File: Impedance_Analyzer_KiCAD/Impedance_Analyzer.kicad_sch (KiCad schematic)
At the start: 39 parts, among them J1 Conn_Coaxial, J10 Conn_Coaxial, J11 Screw_Terminal_01x03, J2 Conn_Coaxial, J3 Conn_Coaxial, J4 Conn_Coaxial, J5 Conn_Coaxial, J6 Conn_Coaxial, J7 Conn_Coaxial, U1 LM358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

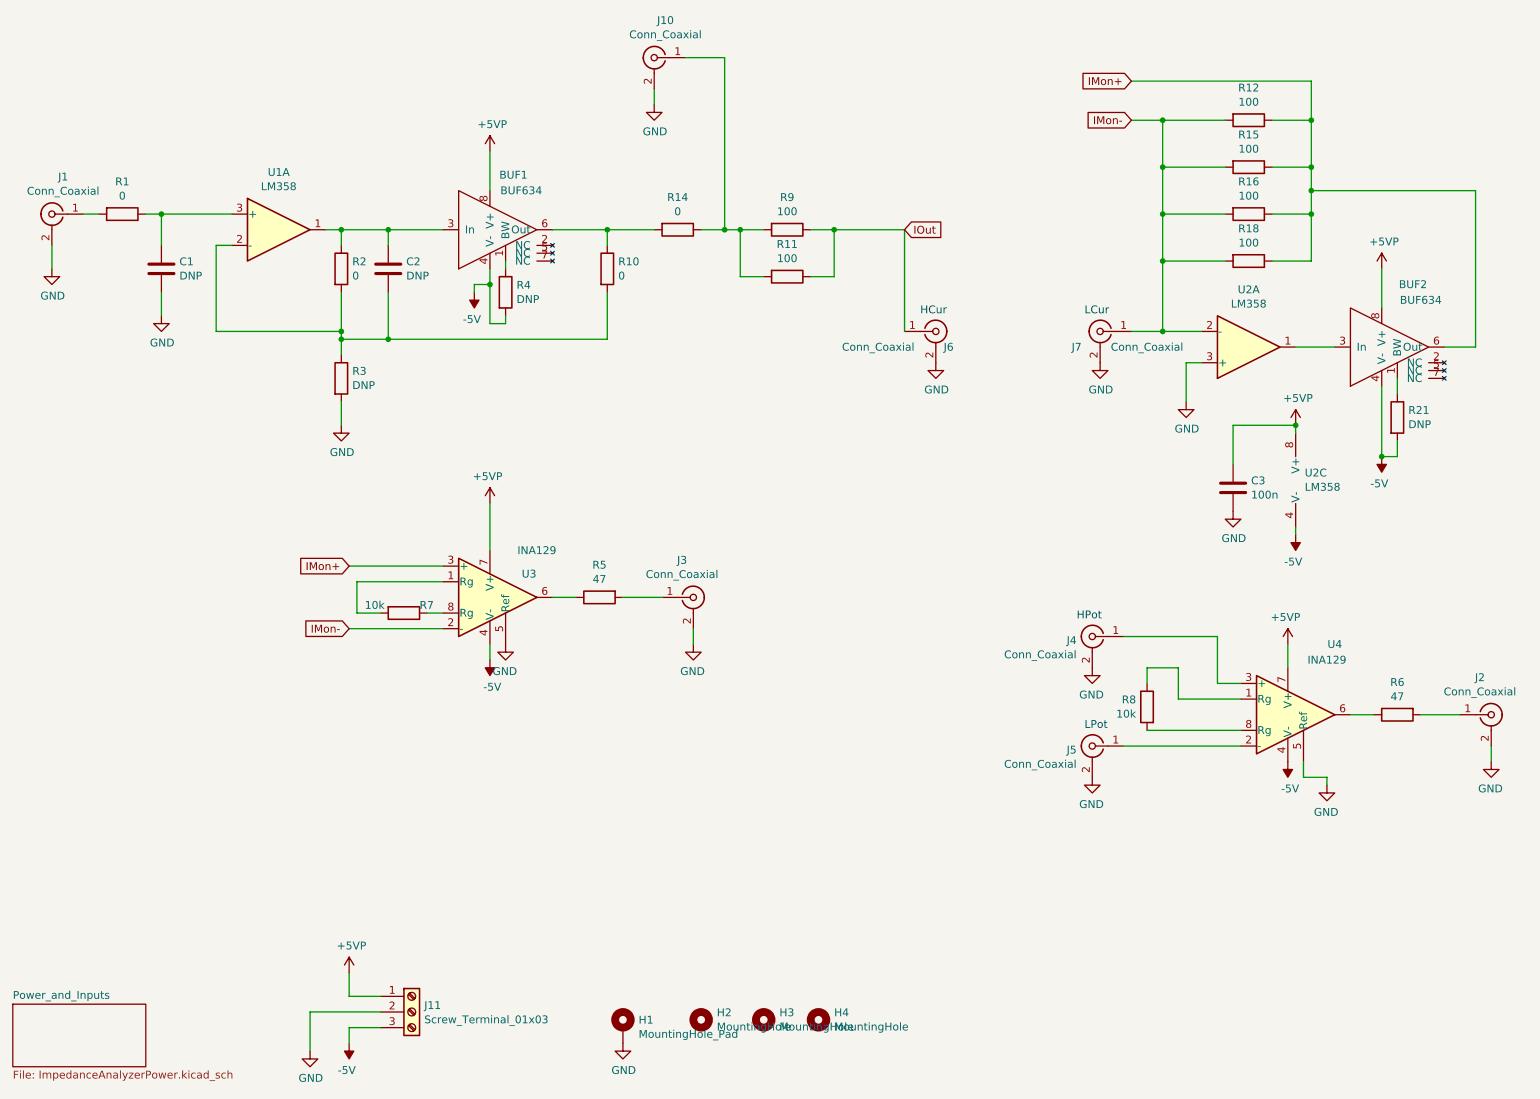
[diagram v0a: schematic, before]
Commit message: Update LTSPICE, Minor board changes
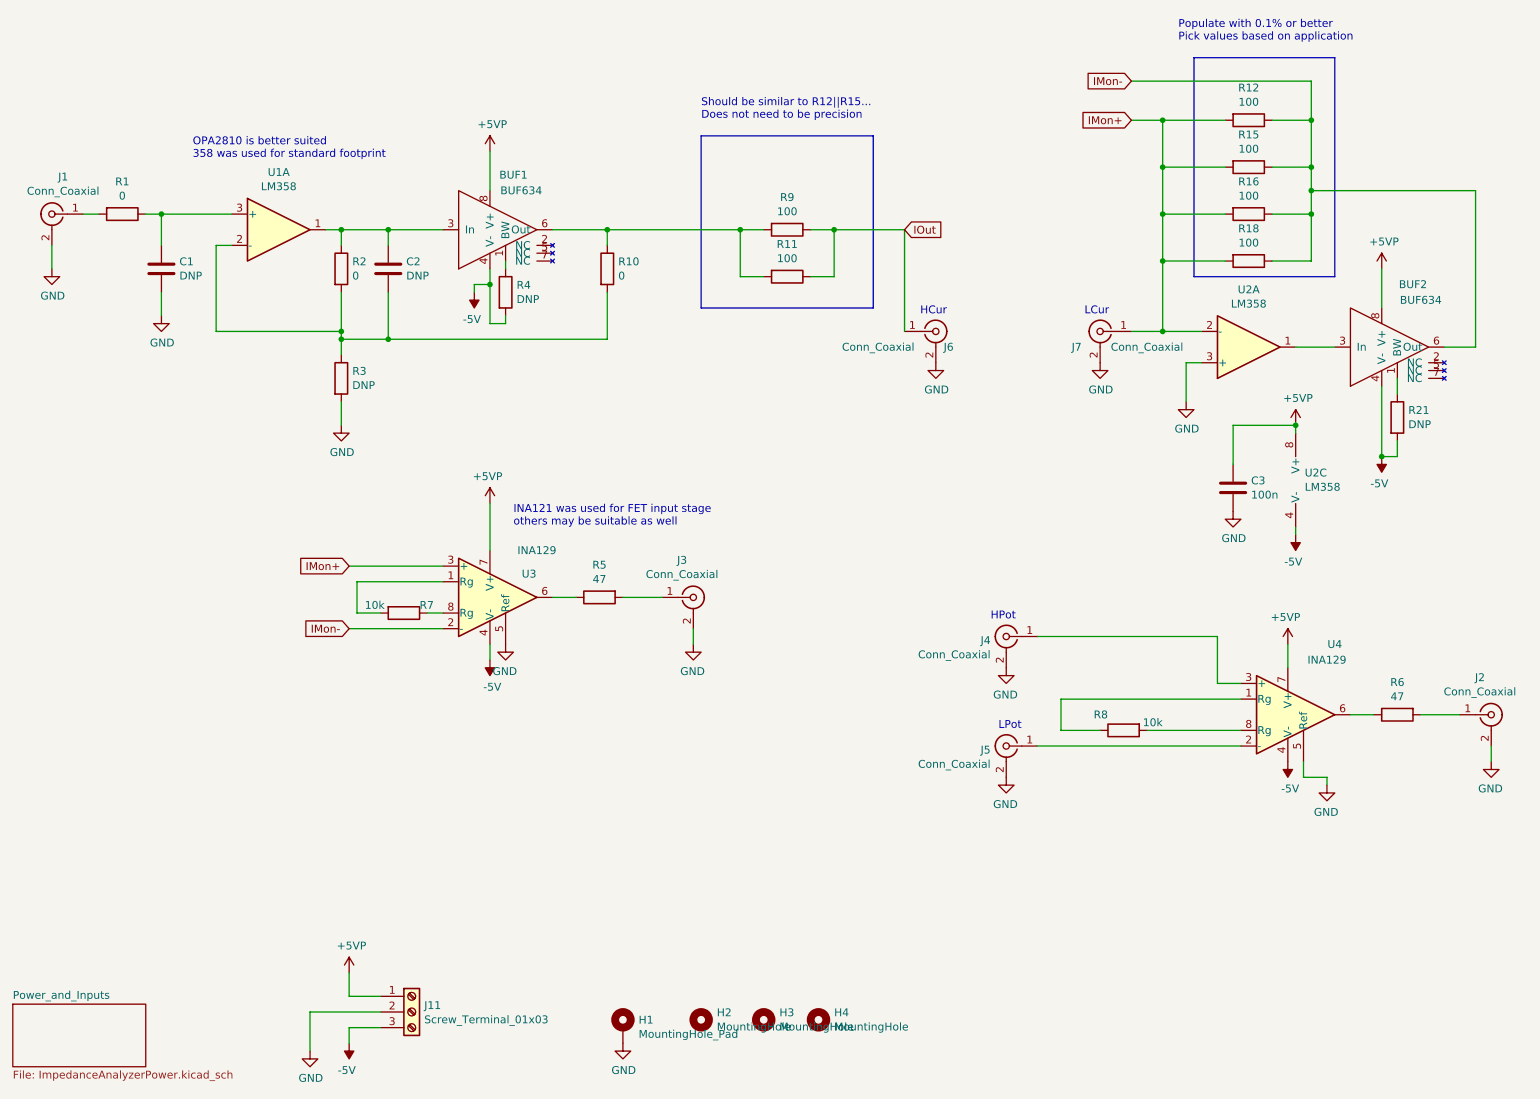
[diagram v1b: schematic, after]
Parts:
- removed J10: Conn_Coaxial, Connector_Coaxial:BNC_TEConnectivity_1478204_Vertical, symbol Connector:Conn_Coaxial
- removed R14: 0, Resistor_SMD:R_1206_3216Metric, symbol Device:R
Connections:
- net IMon+: now also J7.1 (In), R12.2, R15.2, R16.2, R18.2, U2.2 (-); no longer BUF2.6 (Out), R12.1, R15.1, R16.1, R18.1
- net IMon-: now also BUF2.6 (Out), R12.1, R15.1, R16.1, R18.1; no longer J7.1 (In), R12.2, R15.2, R16.2, R18.2, U2.2 (-)
- net at R11.2, R9.2: now also BUF1.6 (Out), R10.1
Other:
- note added: "INA121 was used for FET input stage others may be suitable as well"
- note added: "OPA2810 is better suited 358 was used for standard footprint"
- note added: "Populate with 0.1% or better Pick values based on application"
- note added: "Should be similar to R12||R15... Does not need to be precision"
- moved on the sheet: J4, J5, R8
